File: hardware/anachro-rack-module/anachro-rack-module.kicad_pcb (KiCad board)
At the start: 4 copper layers, 65 parts, among them J1 RACK-GPIO4, J10 RACK-UART, J11 RACK-GPIO4, J12 RACK-JTAG, J13 RACK-JTAG, J2 RACK-GPIO5, J3 8P8C, J4 8P8C, J5 RACK-POWER, J6 FPGA-A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

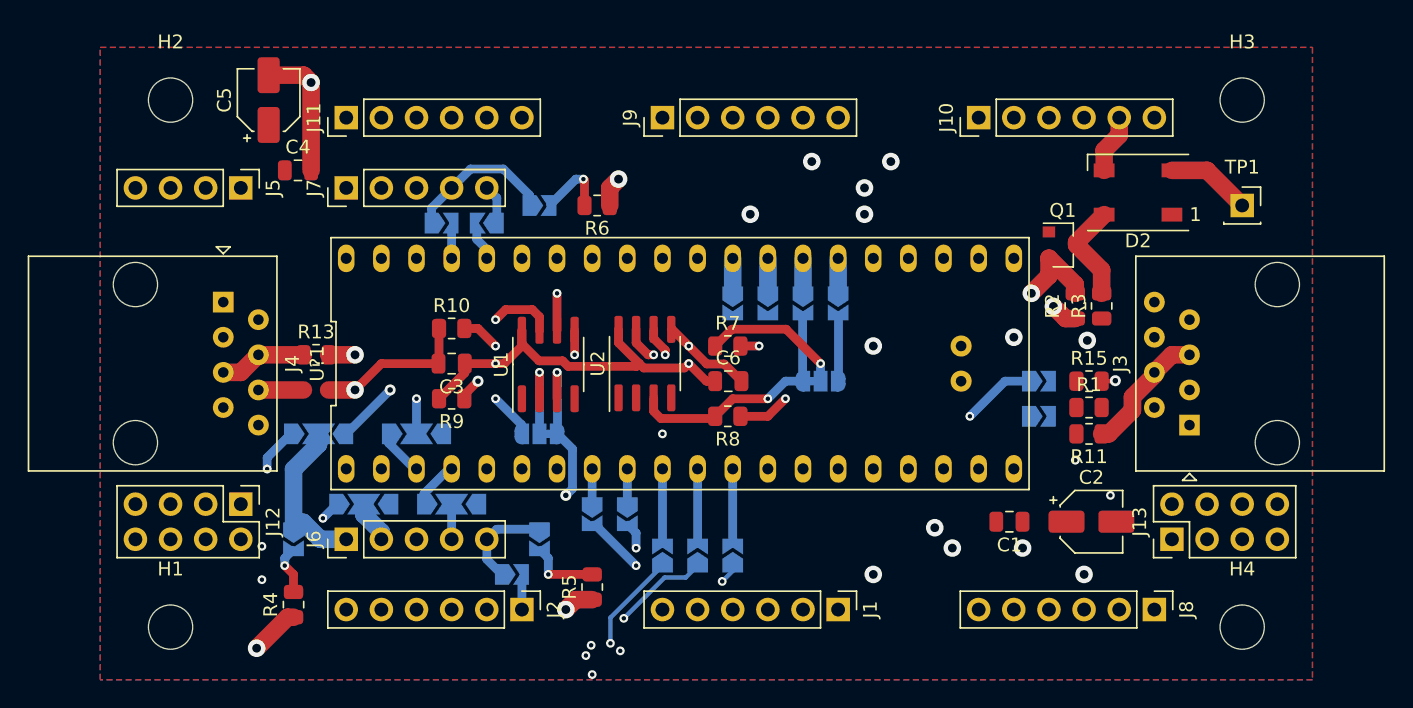
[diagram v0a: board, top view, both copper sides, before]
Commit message: Anachro test rack v2, plus fixed level shifter
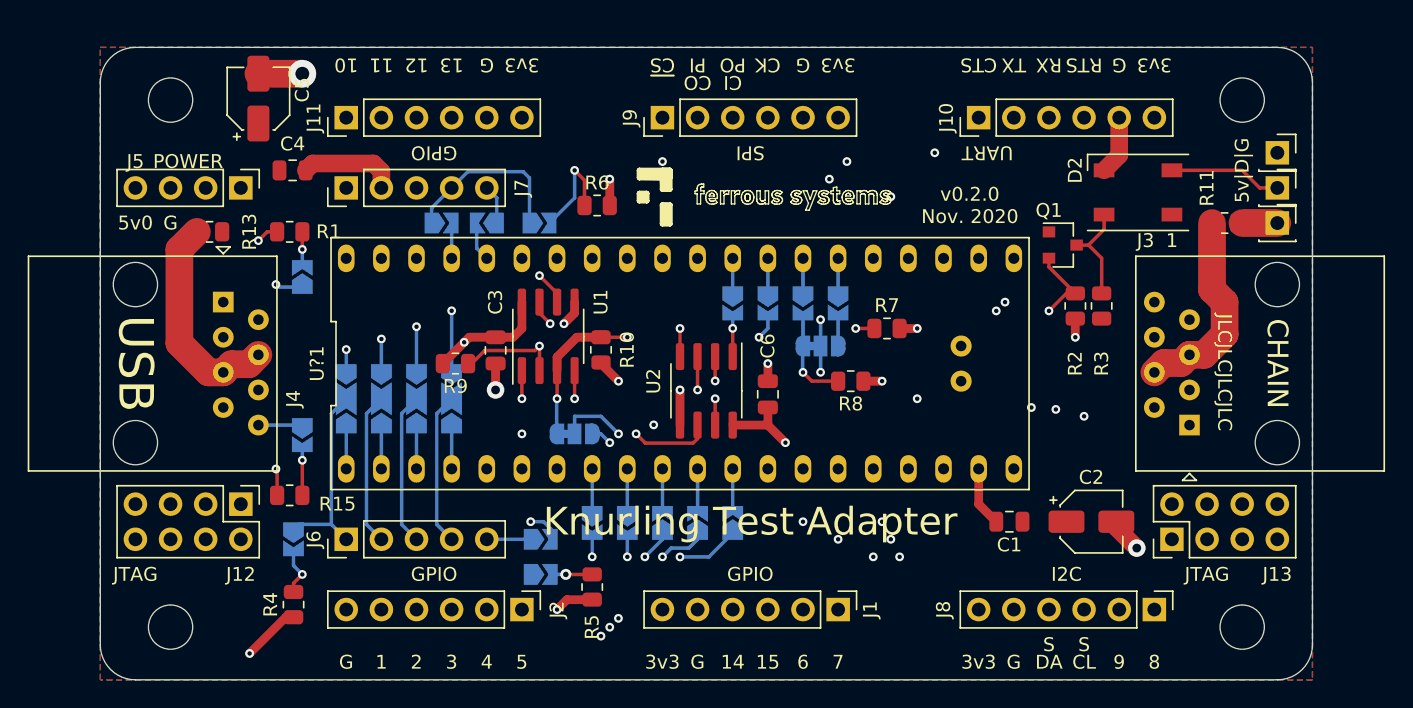
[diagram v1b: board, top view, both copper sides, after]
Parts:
- added TP2: TestPoint, Connector_PinSocket_2.54mm:PinSocket_1x01_P2.54mm_Vertical, F.Cu at (156.2, 55.9)
- added TP3: TestPoint, Connector_PinSocket_2.54mm:PinSocket_1x01_P2.54mm_Vertical, F.Cu at (156.2, 61.0)
- moved R1 59.2 mm to (84.8, 61.6), turned to 180 degrees
- moved R15 58.4 mm to (84.8, 80.6), turned to 180 degrees
- moved JP22 54.2 mm to (85.7, 64.9), turned to 90 degrees
- moved JP23 53.4 mm to (85.7, 76.3), turned to 270 degrees
- moved R11 18.1 mm to (152.4, 61.0), turned to 0 degrees
- moved R13 11.8 mm to (79.0, 61.6)
- moved R7 11.6 mm to (128.0, 68.6)
- moved R10 10.9 mm to (107.3, 70.1), turned to 90 degrees
- moved R8 9.25 mm to (125.4, 72.4)
- moved JP13 7.73 mm to (91.4, 73.7), turned to 90 degrees
- moved JP15 7.62 mm to (96.5, 73.7), turned to 90 degrees
- moved U2 4.86 mm to (114.9, 73.1), turned to 270 degrees
- moved C3 3.32 mm to (99.7, 70.2), turned to 270 degrees
- moved JP9 3.29 mm to (103.0, 83.8)
- moved JP12 3.23 mm to (88.9, 73.7), turned to 90 degrees
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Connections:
- net /FPGA-CDONE renamed /~FPGA-RST
- J6 pad 5: /~FPGA-CRESET -> /FPGA-CLK
- JP9 pad 1: /~FPGA-CRESET -> /FPGA-CLK
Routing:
- net /SPI-SCK: track 13.3 -> 38.4 mm, vias 0 -> 1
- net /SPI-CIPO: track 13.3 -> 33.8 mm, vias 0 -> 1
- net /SPI-COPI: track 13.3 -> 29.4 mm, vias 0 -> 1
- net /Z_OUT: track 99.1 -> 83.1 mm, vias 3 -> 4
- net +3V3: track 40.0 -> 25.9 mm
- net /GPIO9: track 55.6 -> 43.3 mm
- net /GPIO1: track 25.7 -> 14.3 mm, vias 1 -> 0
- net Net-(JP21-Pad2): track 0.00 -> 10.0 mm, vias 0 -> 2
- net /~SWD-RST: track 134.2 -> 124.6 mm
- net Net-(J4-Pad4): track 6.32 -> 15.7 mm
- net /GPIO11: track 25.3 -> 16.2 mm
- net Net-(JP19-Pad2): track 12.7 -> 21.5 mm
- net /RS-485-TX: track 0.00 -> 8.68 mm, vias 0 -> 1
- net /FPGA-COPI: track 2.54 -> 11.1 mm
- net GND: track 40.6 -> 32.2 mm, vias 5 -> 8
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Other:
- board outline added: 87.6 x 45.7 mm
- board text added: "1"
- board text added: "10"
- board text added: "11"
- board text added: "12"
- board text added: "13"
- board text added: "14"
- board text added: "15"
- board text added: "2"
- board text added: "3"
- board text added: "3v3"
- board text added: "4"
- board text added: "5"
- board text added: "5v0"
- board text added: "5v|D|G"
- board text added: "6"
- board text added: "7"
- board text added: "8"
- board text added: "9"
- board text added: "CHAIN"
- board text added: "CI"
- board text added: "CK"
- board text added: "CL"
- board text added: "CO"
- board text added: "CTL"
- board text added: "CTS"
- board text added: "DA"
- board text added: "FPGA"
- board text added: "FPGA SPI"
- board text added: "G"
- board text added: "GPIO"
- board text added: "I2C"
- board text added: "JLCJLCJLCJLC"
- board text added: "JTAG"
- board text added: "Knurling Test Adapter"
- board text added: "PI"
- board text added: "PO"
- board text added: "POWER"
- board text added: "RS485 2"
- board text added: "RS485 TERM"
- board text added: "RTS"
- board text added: "RX"
- board text added: "S"
- board text added: "SPI"
- board text added: "SPI1|SPI2"
- board text added: "TX"
- board text added: "UART"
- board text added: "USB"
- board text added: "v0.2.0 Nov. 2020"
- board text added: "~CS"
- board text added: "~RE1"
- board text added: "~RE2 CTL"
- board text added: "~USB"
